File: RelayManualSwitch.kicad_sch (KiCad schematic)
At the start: 25 parts, among them SW2-1 SW_SPDT, SW2-2 SW_SPDT, SW2-3 SW_SPDT, SW2-4 SW_SPDT, SW2-5 SW_SPDT, SW2-6 SW_SPDT, SW2-7 SW_SPDT, SW2-8 SW_SPDT, SW2-9 MS611F, U2-1 TLP222G-2, U2-2 TLP222G-2, U2-3 TLP222G-2, U2-4 TLP222G-2, U2-5 TLP222G-2, U2-6 TLP222G-2, U2-7 TLP222G-2, U2-8 TLP222G-2

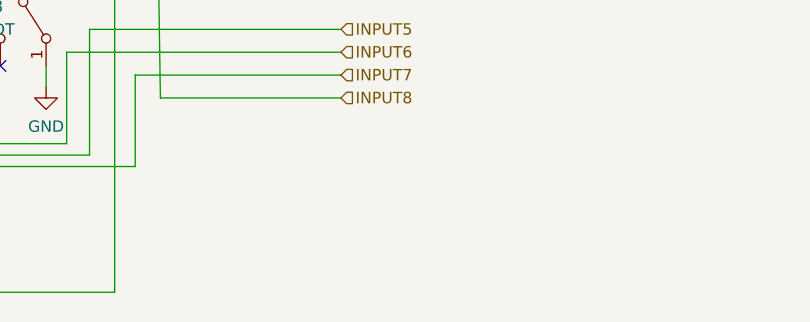
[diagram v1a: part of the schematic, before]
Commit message: InputSwitchのスイッチ名称の変更が必要
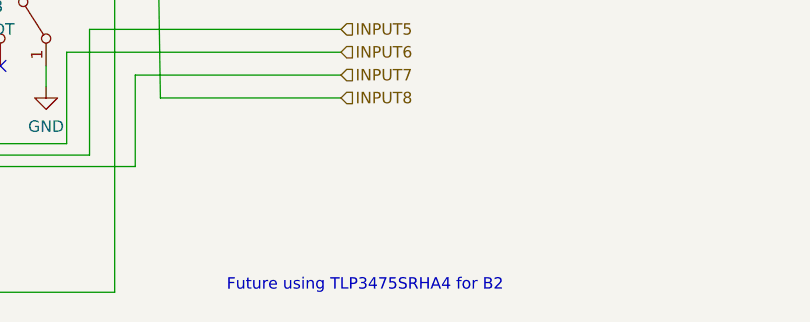
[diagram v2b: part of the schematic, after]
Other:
- note added: "Future using TLP3475SRHA4 for B2"
- company: (none) -> LLC. YS-Lab
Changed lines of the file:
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@@
   (title_block
     (title "Relay Control AUTO/MANUAL")
-    (date "2022-07-08")
-    (rev "1.00")
+    (date "2024-02-16")
+    (rev "1.01")
+    (company "LLC. YS-Lab")
   )
   (junction (at 195.58 33.02) (diameter 0) (color 0 0 0 0)
@@
     (effects (font (size 1.27 1.27)) (justify left bottom))
   )
+  (text "Future using TLP3475SRHA4 for B2" (at 180.34 175.26 0)
+    (effects (font (size 1.27 1.27)) (justify left bottom))
+  )

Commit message: PCB配置作業中
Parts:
- renumbered D2-2 to D2-202, D2-1 to D201, D2-3 to D203, R2-1 to R201, R2-2 to R202, R2-3 to R203, RN2-1 to RN201, RN2-2 to RN202, SW2-1 to SW201, SW2-5 to SW202, SW2-2 to SW203, SW2-6 to SW204, SW2-3 to SW205, SW2-7 to SW206, SW2-4 to SW207, SW2-8 to SW208, SW2-9 to SW209, U2-1 to U201, U2-5 to U202, U2-2 to U203, U2-6 to U204, U2-3 to U205, U2-7 to U206, U2-4 to U207, U2-8 to U208
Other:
- moved on the sheet: RN201, RN202, SW201, SW202, SW203, SW204, SW205, SW206, SW207, SW208, U201, U202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
